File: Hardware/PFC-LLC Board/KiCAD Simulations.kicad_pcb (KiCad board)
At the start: 2 copper layers, 28 parts, among them Q1 C2M0160120D, U1 UCC28180DR

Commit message: Start of PCB
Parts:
- added C16: 220p, Capacitor_SMD:C_0402_1005Metric_Pad0.74x0.62mm_HandSolder, F.Cu at (81.3, 69.8)
- added Cboot1: 220n, Capacitor_SMD:C_0603_1608Metric_Pad1.08x0.95mm_HandSolder, F.Cu at (87.6, 221.0)
- added Cbw1: 3.9p, Capacitor_SMD:C_0402_1005Metric_Pad0.74x0.62mm_HandSolder, F.Cu at (42.5, 246.0)
- added Ccomp3: 390n, Capacitor_SMD:C_1206_3216Metric_Pad1.33x1.80mm_HandSolder, F.Cu at (67.3, 221.4)
- added Cin2: 47u, Capacitor_THT:CP_Radial_D25.0mm_P10.00mm_SnapIn, F.Cu at (47.0, 58.6)
- added Cinx1: 1.5u, Capacitor_THT:C_Rect_L26.5mm_W10.5mm_P22.50mm_MKS4, F.Cu at (71.1, 52.4)
- added Cisns1: 3.3p, Capacitor_SMD:C_0402_1005Metric_Pad0.74x0.62mm_HandSolder, F.Cu at (108.7, 127.0)
- added Cisns2: 150p, LLC_Cisns2:FA26C0G2J151JNU00, F.Cu at (157.5, 50.8)
- added Cout21: 120u, LLC_Cout:35SVPF120M, F.Cu at (242.6, 24.1)
- added Cout22: 120u, LLC_Cout:35SVPF120M, F.Cu at (242.6, 38.1)
- added Cout23: 120u, LLC_Cout:35SVPF120M, F.Cu at (242.6, 50.8)
- added Cout24: 120u, LLC_Cout:35SVPF120M, F.Cu at (242.6, 63.5)
- added Cout25: 120u, LLC_Cout:35SVPF120M, F.Cu at (242.6, 76.2)
- added Cout26: 120u, LLC_Cout:35SVPF120M, F.Cu at (243.1, 88.9)
- added Coutx21: 22u, Capacitor_SMD:C_0805_2012Metric_Pad1.18x1.45mm_HandSolder, F.Cu at (259.1, 31.8)
- added Coutx22: 22u, Capacitor_SMD:C_0805_2012Metric_Pad1.18x1.45mm_HandSolder, F.Cu at (259.3, 39.4)
- added Coutx23: 22u, Capacitor_SMD:C_0805_2012Metric_Pad1.18x1.45mm_HandSolder, F.Cu at (259.1, 45.7)
- added Coutx24: 22u, Capacitor_SMD:C_0805_2012Metric_Pad1.18x1.45mm_HandSolder, F.Cu at (259.1, 52.1)
- added Cr1: 33.454n, Capacitor_THT:C_Rect_L13.0mm_W5.0mm_P10.00mm_FKS3_FKP3_MKS4, F.Cu at (127.0, 50.8)
- added Cr2: 33.454n, Capacitor_THT:C_Rect_L13.0mm_W5.0mm_P10.00mm_FKS3_FKP3_MKS4, F.Cu at (127.0, 64.8)
- added Creg1: 2.2u, Capacitor_SMD:C_0402_1005Metric_Pad0.74x0.62mm_HandSolder, F.Cu at (181.6, 66.0)
- added Crvcc2: 4.7u, Capacitor_SMD:C_0805_2012Metric_Pad1.18x1.45mm_HandSolder, F.Cu at (52.0, 234.5)
- added Css1: 47n, Capacitor_SMD:C_0402_1005Metric_Pad0.74x0.62mm_HandSolder, F.Cu at (60.2, 231.9)
- added Css11: 47n, Capacitor_SMD:C_0402_1005Metric_Pad0.74x0.62mm_HandSolder, F.Cu at (109.9, 259.7)
- added Css12: 47n, Capacitor_SMD:C_0402_1005Metric_Pad0.74x0.62mm_HandSolder, F.Cu at (113.1, 259.7)
- added Css13: 47n, Capacitor_SMD:C_0402_1005Metric_Pad0.74x0.62mm_HandSolder, F.Cu at (98.5, 237.6)
- added Cvcc21: 15u, Capacitor_SMD:CP_Elec_5x5.8, F.Cu at (27.9, 134.6)
- added Cvcc22: 15u, Capacitor_SMD:CP_Elec_5x5.8, F.Cu at (38.1, 134.6)
- added Cvcc23: 15u, Capacitor_SMD:CP_Elec_5x5.8, F.Cu at (48.3, 134.6)
- added Cvcc24: 15u, Capacitor_SMD:CP_Elec_5x5.8, F.Cu at (58.4, 134.6)
- added Cvcc25: 15u, Capacitor_SMD:CP_Elec_5x5.8, F.Cu at (68.6, 134.6)
- added Cvcc26: 15u, Capacitor_SMD:CP_Elec_5x5.8, F.Cu at (78.7, 134.6)
- added Cvcc27: 15u, Capacitor_SMD:CP_Elec_5x5.8, F.Cu at (88.9, 134.6)
- added Cvcc28: 15u, Capacitor_SMD:CP_Elec_5x5.8, F.Cu at (99.1, 134.6)
- added Cvcc3: 2.2u, Capacitor_SMD:C_0805_2012Metric_Pad1.18x1.45mm_HandSolder, F.Cu at (109.2, 134.6)
- added Cvcr1: 66.044p, Capacitor_THT:C_Rect_L7.2mm_W4.5mm_P5.00mm_FKS2_FKP2_MKS2_MKP2, F.Cu at (144.9, 57.1)
- added Cvcr2: 1n, Capacitor_SMD:C_0805_2012Metric_Pad1.18x1.45mm_HandSolder, F.Cu at (48.1, 240.5)
- added Cvcr21: 1n, Capacitor_SMD:C_0805_2012Metric_Pad1.18x1.45mm_HandSolder, F.Cu at (147.3, 66.0)
- added Cvcr22: 1n, Capacitor_SMD:C_0805_2012Metric_Pad1.18x1.45mm_HandSolder, F.Cu at (147.3, 71.1)
- added Cvcr23: 1n, Capacitor_SMD:C_0805_2012Metric_Pad1.18x1.45mm_HandSolder, F.Cu at (147.3, 74.9)
- added Cvcr24: 1n, Capacitor_SMD:C_0805_2012Metric_Pad1.18x1.45mm_HandSolder, F.Cu at (147.6, 80.0)
- added Cvcr25: 1n, Capacitor_SMD:C_0805_2012Metric_Pad1.18x1.45mm_HandSolder, F.Cu at (147.3, 85.1)
- added Cvcr26: 1n, Capacitor_SMD:C_0805_2012Metric_Pad1.18x1.45mm_HandSolder, F.Cu at (147.6, 90.2)
- added Cvrcc1: 4.7u, Capacitor_SMD:C_0805_2012Metric_Pad1.18x1.45mm_HandSolder, F.Cu at (43.3, 243.5)
- added Cz1: 100n, Capacitor_SMD:C_0603_1608Metric_Pad1.08x0.95mm_HandSolder, F.Cu at (83.3, 221.0)
- added Dboot1: DIODE, DO-214BA:DO-214BA, F.Cu at (55.0, 254.1)
- added Dz1: BZX84Cxx, Diode_SMD:D_SOT-23_ANK, F.Cu at (52.8, 241.2)
- added J1: Conn_01x02_Female, Connector_PinHeader_1.27mm:PinHeader_1x02_P1.27mm_Vertical, F.Cu at (110.5, -39.4)
- added J2: Conn_01x02_Female, Connector_PinHeader_1.27mm:PinHeader_1x02_P1.27mm_Vertical, F.Cu at (47.8, 243.7)
- added J3: Conn_01x02_Female, Connector_PinHeader_1.27mm:PinHeader_1x02_P1.27mm_Vertical, F.Cu at (56.5, 232.0)
- added QM1: IPP060N06N, Package_TO_SOT_THT:TO-220-3_Vertical, F.Cu at (113.0, 52.1)
- added QM2: IPP060N06N, Package_TO_SOT_THT:TO-220-3_Vertical, F.Cu at (113.0, 66.0)
- added QM3: C2M0025120D, Package_TO_SOT_THT:TO-247-3_Vertical, F.Cu at (172.7, 53.3)
- added QM4: C2M0025120D, Package_TO_SOT_THT:TO-247-3_Vertical, F.Cu at (215.5, 66.0)
- added R19: 121k, Resistor_SMD:R_0402_1005Metric_Pad0.72x0.64mm_HandSolder, F.Cu at (81.3, 67.3)
- added R20: 4.99M, Resistor_SMD:R_1206_3216Metric_Pad1.30x1.75mm_HandSolder, F.Cu at (82.3, 52.1)
- added R27: 4.99M, Resistor_SMD:R_1206_3216Metric_Pad1.30x1.75mm_HandSolder, F.Cu at (82.3, 62.2)
- added R28: 4.99M, Resistor_SMD:R_1206_3216Metric_Pad1.30x1.75mm_HandSolder, F.Cu at (82.3, 57.1)
- added Rbias1: 6.04k, Resistor_SMD:R_0402_1005Metric_Pad0.72x0.64mm_HandSolder, F.Cu at (66.0, 211.8)
- added Rboot1: 2.20, Resistor_SMD:R_0805_2012Metric_Pad1.20x1.40mm_HandSolder, F.Cu at (52.0, 237.4)
- added Rbw1: 35.7k, Resistor_SMD:R_0402_1005Metric_Pad0.72x0.64mm_HandSolder, F.Cu at (161.3, 66.0)
- added Rbw2: 10k, Resistor_SMD:R_0201_0603Metric_Pad0.64x0.40mm_HandSolder, F.Cu at (161.3, 72.4)
- added Rcomp2: 44.2k, Resistor_SMD:R_0201_0603Metric_Pad0.64x0.40mm_HandSolder, F.Cu at (72.2, 211.7)
- added Rdrv1: 5.11k, Resistor_SMD:R_0402_1005Metric_Pad0.72x0.64mm_HandSolder, F.Cu at (97.8, 57.1)
- added Rdrv2: 5.11k, Resistor_SMD:R_0402_1005Metric_Pad0.72x0.64mm_HandSolder, F.Cu at (98.4, 67.3)
- added Rfbb2: 8.06k, Resistor_SMD:R_0402_1005Metric_Pad0.72x0.64mm_HandSolder, F.Cu at (69.2, 211.8)
- added Rfbt4: 110k, Resistor_SMD:R_0603_1608Metric_Pad0.98x0.95mm_HandSolder, F.Cu at (61.0, 252.5)
- added Rho1: 1, Resistor_SMD:R_0402_1005Metric_Pad0.72x0.64mm_HandSolder, F.Cu at (98.4, 52.1)
- added Risns1: 80.759, Resistor_SMD:R_0603_1608Metric_Pad0.98x0.95mm_HandSolder, F.Cu at (157.8, 57.1)
- added Rled1: 36.5k, Resistor_SMD:R_0201_0603Metric_Pad0.64x0.40mm_HandSolder, F.Cu at (75.0, 211.7)
- added Rlimit1: 18.2k, Resistor_SMD:R_1206_3216Metric_Pad1.30x1.75mm_HandSolder, F.Cu at (73.3, 221.4)
- added Rlo1: 1, Resistor_SMD:R_0402_1005Metric_Pad0.72x0.64mm_HandSolder, F.Cu at (98.4, 62.2)
- added Rvcc1: 44.2k, Resistor_SMD:R_0201_0603Metric_Pad0.64x0.40mm_HandSolder, F.Cu at (60.0, 233.8)
- added Rvcc2: 12.1k, Resistor_SMD:R_0201_0603Metric_Pad0.64x0.40mm_HandSolder, F.Cu at (55.8, 237.8)
- added U1LLC1: UCC256403DDBR, LLC_U1:UCC256403DDBR, F.Cu at (101.6, 94.0)
- added U2LLC1: UCC24624DT, LLC_U2:UCC24624DT, F.Cu at (199.4, 62.2)
- added UO1: PS2501L-1-F3-A, LLC_O1:PS2501L-1-F3-A, F.Cu at (157.5, 208.3)
- added UVR1: TLV431AIDBVT, LLC_VR1:TLV431AIDBVT, F.Cu at (71.6, 243.9)
- moved Ccomp1 146.8 mm to (76.2, -61.0)
- moved Ccomp2 146.8 mm to (88.0, -64.4)
- moved Cicomp1 146.8 mm to (81.0, -61.0)
- moved Cin1 146.8 mm to (76.2, -58.0)
- moved Cisense1 146.8 mm to (83.3, -56.8)
- moved Cvcc1 146.8 mm to (70.8, -60.8)
- moved Cvsense1 146.8 mm to (83.3, -58.6)
- moved Dac1 146.8 mm to (95.9, -67.0)
- moved Dboost1 146.8 mm to (87.6, -53.3)
- moved Disense1 146.8 mm to (117.0, -67.7)
- moved Dstart1 146.8 mm to (87.6, -41.9)
- moved Dturnoff1 146.8 mm to (142.6, -52.1)
- moved Q1 146.8 mm to (115.0, -60.9)
- moved Rcomp1 146.8 mm to (80.0, -56.6)
- moved Rfbb1 146.8 mm to (91.0, -66.5)
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
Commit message: Schematic/PCB updates
Minor updates to schematic and some place of PCB components as been done
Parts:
- removed Css1: 47n, Capacitor_SMD:C_0402_1005Metric_Pad0.74x0.62mm_HandSolder
- removed Dac1: GBU8M, Diode_THT:Diode_Bridge_Vishay_GBU
- removed the U1 at (132.5, -41.4)
- moved Cout21 221.3 mm to (268.7, 243.8), turned to 270 degrees
- moved Cout22 206.2 mm to (256.0, 243.8), turned to 270 degrees
- moved Cout23 193.0 mm to (243.3, 243.8), turned to 270 degrees
- moved Rbw1 191.2 mm to (94.2, 245.1), turned to 180 degrees
- moved Rbw2 183.9 mm to (94.1, 243.6)
- moved Cvcc28 181.6 mm to (31.0, 303.0), turned to 270 degrees
- moved Coutx21 181.6 mm to (278.4, 212.3)
- moved Coutx22 178.1 mm to (278.4, 216.4)
- moved Rho1 176.5 mm to (100.0, 228.6)
- moved Coutx23 175.8 mm to (278.4, 220.5)
- moved Cvcc27 175.0 mm to (41.1, 303.0), turned to 270 degrees
- moved Cr1 174.5 mm to (113.8, 224.8), turned to 270 degrees
- moved Coutx24 173.5 mm to (278.4, 224.5)
- moved Rlo1 173.0 mm to (100.1, 235.2)
- moved Cvcc26 170.6 mm to (51.3, 303.0), turned to 270 degrees
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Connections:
- Ccomp2 pad 2: Net-(Ccomp2-Pad2) -> GND
- Cicomp1 pad 2: Net-(Ccomp2-Pad2) -> GND
- Cisense1 pad 2: Net-(Ccomp2-Pad2) -> GND
- Cvcc1 pad 2: Net-(Ccomp2-Pad2) -> GND
- Cvccx1 pad 2: Net-(Ccomp2-Pad2) -> GND
- Cvsense1 pad 2: Net-(Ccomp2-Pad2) -> GND
- Disense1 pad 2: Net-(Ccomp2-Pad2) -> GND
- J1 pad 1: Net-(Ccomp2-Pad2) -> GND
- Rcomp1 pad 2: Net-(Ccomp2-Pad2) -> GND
- Rfbb1 pad 2: Net-(Ccomp2-Pad2) -> GND
- Rfreq1 pad 2: Net-(Ccomp2-Pad2) -> GND
- U1 pad 1: Net-(Ccomp2-Pad2) -> GND

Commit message: All footprints except PFC output caps
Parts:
- removed Cvcr2: 1n, Capacitor_SMD:C_0805_2012Metric_Pad1.18x1.45mm_HandSolder
- removed J1, J2, J3: Conn_01x02_Female, Connector_PinHeader_1.27mm:PinHeader_1x02_P1.27mm_Vertical
- added L1: 148.268u, PFC_L1:IND_FIT106-2, F.Cu at (275.6, -52.6)
- added Lr1: PA4344.473ANLT, LLC_Lr:PA4344.473ANLT, F.Cu at (331.2, 117.3)
- added Rntc1: 1, Resistor_THT:R_Box_L13.0mm_W4.0mm_P9.00mm, F.Cu at (187.2, -19.8)
- added TR1: TRANSF6, LLC_T1:EPCOS-B65982E0012D001-MFG, F.Cu at (351.5, 49.8)
- moved Cvcc24 220.3 mm to (181.9, 133.6), turned to 90 degrees
- moved Cvcc23 206.9 mm to (171.7, 133.6), turned to 90 degrees
- moved Rvcc1 201.6 mm to (198.4, 145.6)
- moved Css11 200.9 mm to (193.3, 145.5)
- moved Css12 200.9 mm to (190.8, 145.5)
- moved Css13 200.9 mm to (188.2, 145.5)
- moved Rvcc2 200.9 mm to (195.8, 145.6)
- moved Cbw1 200.5 mm to (197.1, 132.0)
- moved Cisns1 200.5 mm to (193.3, 132.0)
- moved Crvcc2 200.5 mm to (194.3, 137.7)
- moved Cvcc25 200.5 mm to (181.9, 142.7)
- moved Cvcc26 200.5 mm to (171.7, 142.7)
- moved Cvcc27 200.5 mm to (161.5, 142.7)
- moved Cvcc28 200.5 mm to (151.4, 142.7)
- moved Cvcc3 200.5 mm to (189.5, 132.4)
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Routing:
- net GND: track 0.00 -> 59.6 mm
- net Net-(Cvcr1-Pad2): track 0.00 -> 27.7 mm
- net Net-(Rbias1-Pad1): track 0.00 -> 25.0 mm
- net Net-(Rbias1-Pad2): track 0.00 -> 22.7 mm
- net Net-(Cz1-Pad1): track 0.00 -> 16.6 mm
- net Net-(Ccomp3-Pad1): track 0.00 -> 15.9 mm
- net Net-(Css11-Pad1): track 0.00 -> 10.2 mm
- net Net-(Crvcc2-Pad1): track 0.00 -> 9.38 mm
- net Net-(Rfbb2-Pad2): track 0.00 -> 5.39 mm
- net Net-(Cz1-Pad2): track 0.00 -> 4.96 mm
- net Net-(Ccomp3-Pad2): track 0.00 -> 3.73 mm
- net Net-(Cout21-Pad1): track 0.00 -> 3.11 mm
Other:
- board outline added: 217.4 x 136.9 mm

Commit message: missing 4 PFC components
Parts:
- added J1: 1792229, Connector2x1:PHOENIX_1792229, F.Cu at (148.6, -30.5)
- added J2: Conn_01x02_Female, Connector_PinHeader_1.27mm:PinHeader_1x02_P1.27mm_Vertical, F.Cu at (243.3, -26.2)
- added J3: 1792229, Connector2x1:PHOENIX_1792229, F.Cu at (266.2, -17.0)
- added J4: 1792229, Connector2x1:PHOENIX_1792229, F.Cu at (114.6, 136.9)
- added J5: Conn_01x02_Female, Connector_PinHeader_1.27mm:PinHeader_1x02_P1.27mm_Vertical, F.Cu at (141.0, 132.8)
- added J6: 1792229, Connector2x1:PHOENIX_1792229, F.Cu at (114.8, 113.0)
- moved Lr1 140.8 mm to (197.9, 72.1), turned to 270 degrees
- moved TR1 116.9 mm to (238.3, 78.5), turned to 0 degrees
- moved Cout24 30.4 mm to (128.3, 83.6)
- moved Cout25 30.4 mm to (141.0, 83.6)
- moved Cout26 30.4 mm to (115.6, 83.6)
- moved Cout21 30.4 mm to (115.6, 98.0)
- moved Cout22 30.4 mm to (128.3, 98.0)
- moved Cout23 30.4 mm to (141.0, 98.0)
- moved QM3 29.8 mm to (160.3, 53.1)
- moved QM4 29.8 mm to (181.6, 53.1)
- moved Coutx21 29.4 mm to (152.7, 80.3)
- moved Coutx22 29.4 mm to (156.7, 80.3)
- moved Coutx23 29.4 mm to (160.8, 80.3)
- moved Coutx24 29.4 mm to (164.8, 80.3)
- moved Creg1 27.7 mm to (167.1, 75.2)
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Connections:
- Cout21 pad 2: Net-(Cout21-Pad2) -> GND1
- Cout22 pad 2: Net-(Cout21-Pad2) -> GND1
- Cout23 pad 2: Net-(Cout21-Pad2) -> GND1
- Cout24 pad 2: Net-(Cout21-Pad2) -> GND1
- Cout25 pad 2: Net-(Cout21-Pad2) -> GND1
- Cout26 pad 2: Net-(Cout21-Pad2) -> GND1
- Coutx21 pad 2: Net-(Cout21-Pad2) -> GND1
- Coutx22 pad 2: Net-(Cout21-Pad2) -> GND1
- Coutx23 pad 2: Net-(Cout21-Pad2) -> GND1
- Coutx24 pad 2: Net-(Cout21-Pad2) -> GND1
- Creg1 pad 2: Net-(Cout21-Pad2) -> GND1
- Cz1 pad 2: Net-(Cz1-Pad2) -> GND1
- Dz1 pad 2: Net-(Cz1-Pad2) -> GND1
- QM3 pad 2: Net-(Cout21-Pad2) -> GND1
- QM4 pad 3: Net-(Cout21-Pad2) -> GND1
- Rfbb2 pad 2: Net-(Rfbb2-Pad2) -> GND1
- U2LLC1 pad 2: Net-(Cout21-Pad2) -> GND1
- U2LLC1 pad 5: Net-(Cout21-Pad2) -> GND1
- UVR1 pad 5: Net-(Rfbb2-Pad2) -> GND1
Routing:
- net GND1: track 0.00 -> 10.3 mm
- net Net-(Rfbb2-Pad2): track 5.39 -> 0.00 mm
- net Net-(Cz1-Pad2): track 4.96 -> 0.00 mm

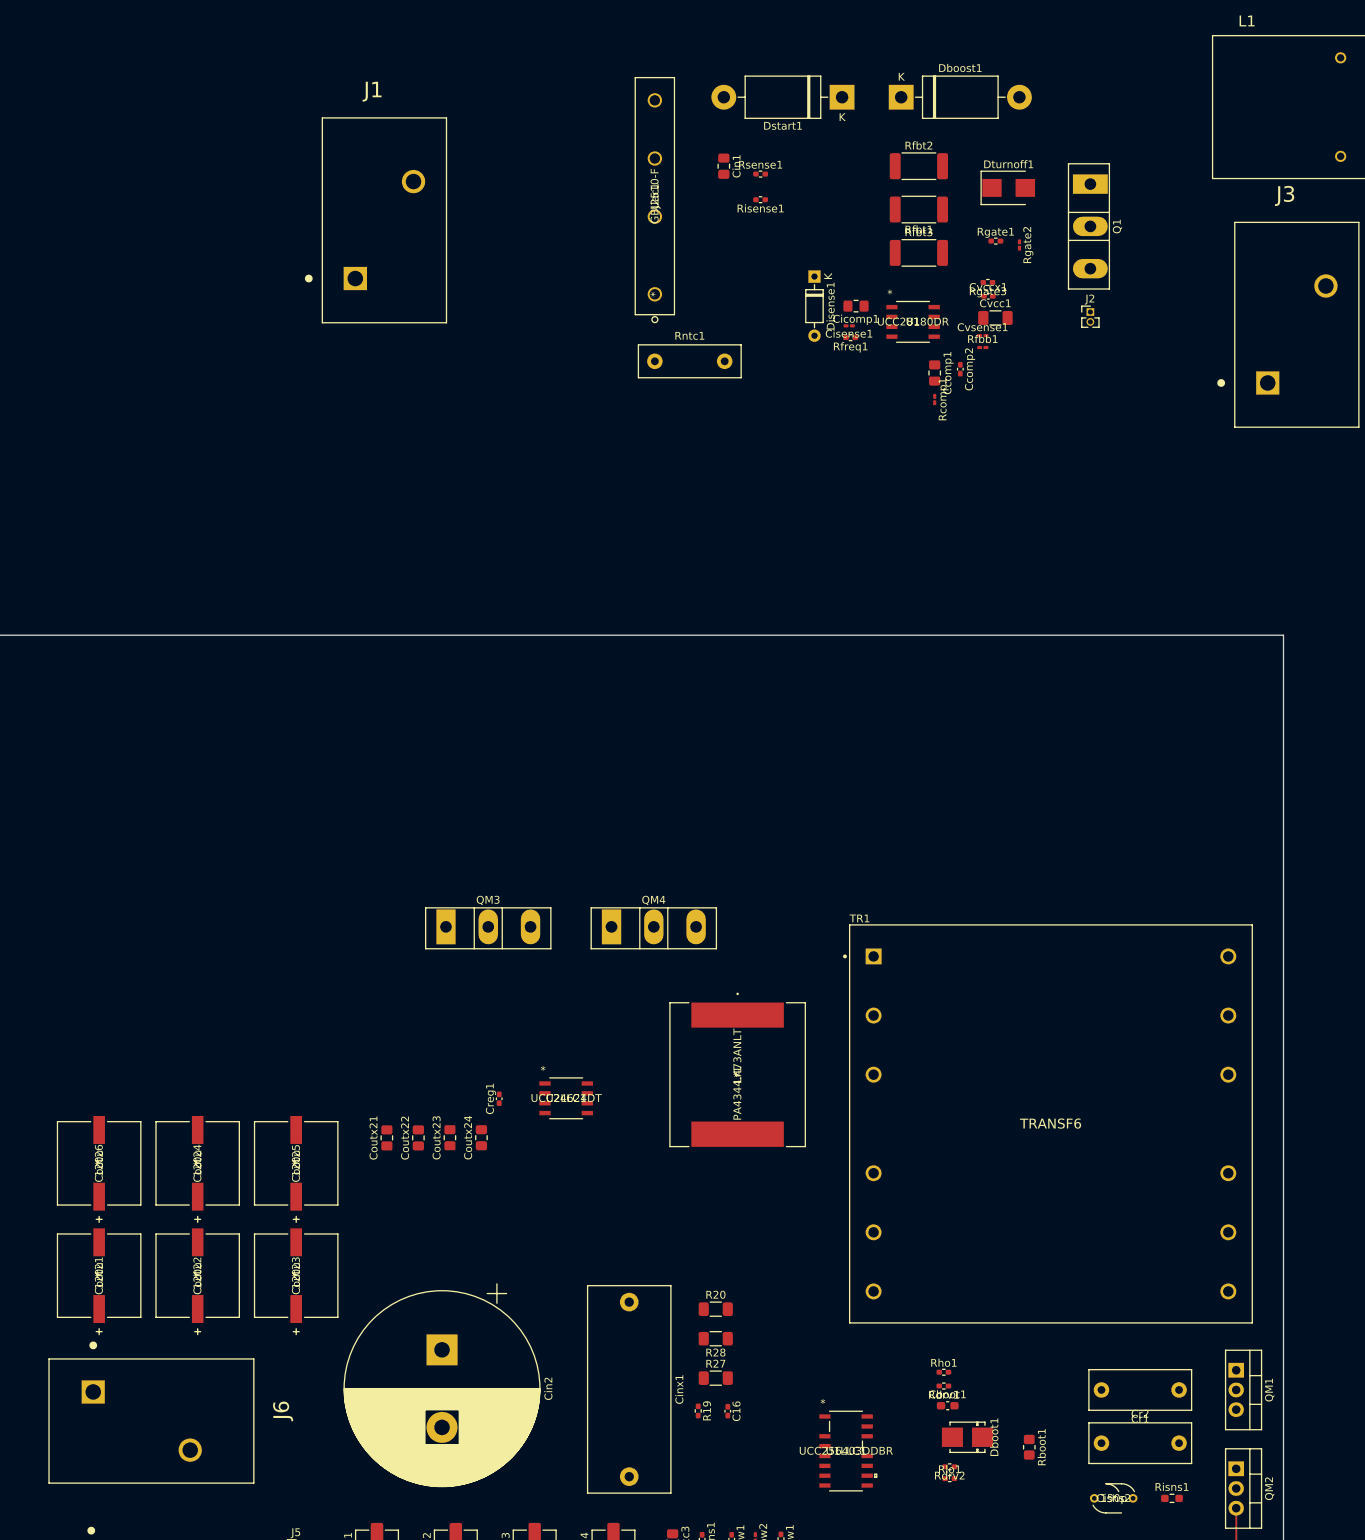
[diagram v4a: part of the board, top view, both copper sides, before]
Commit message: All component footprints found and ready for PCB layout
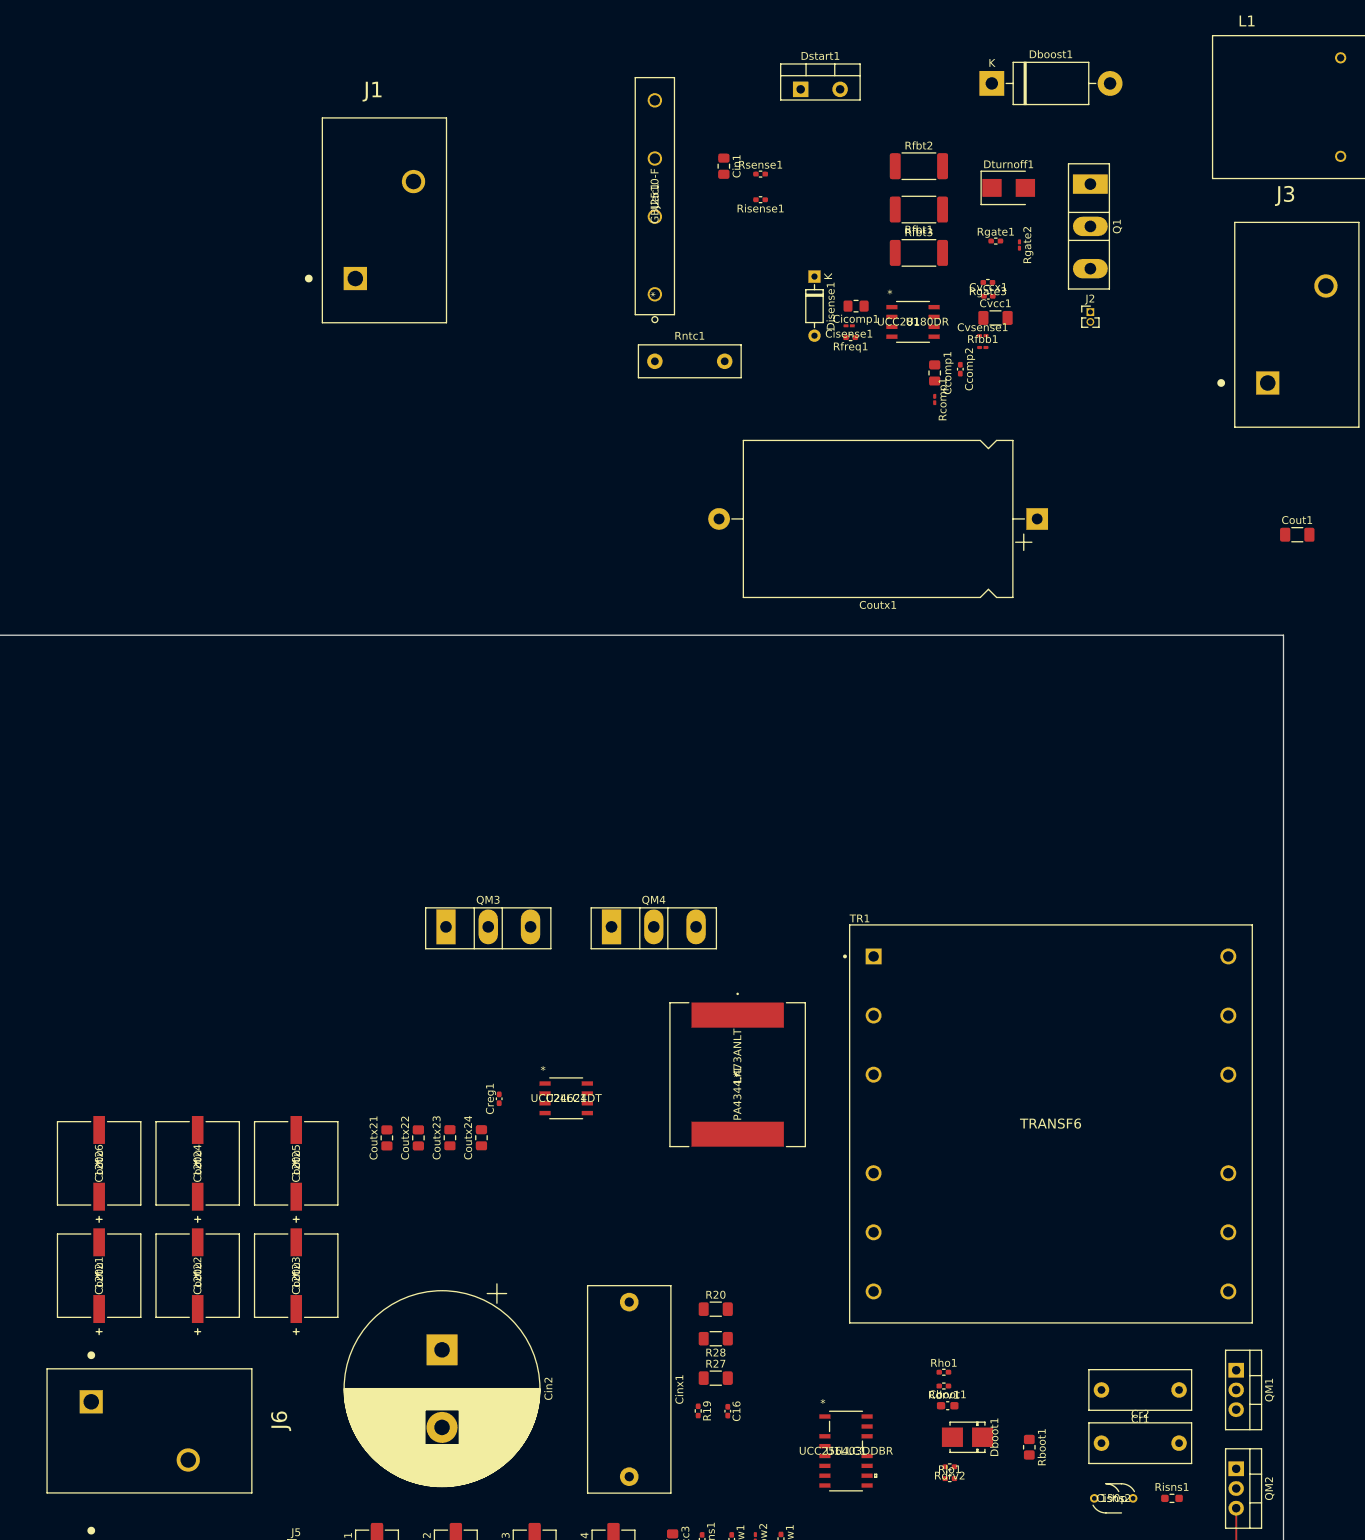
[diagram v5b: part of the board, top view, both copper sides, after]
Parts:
- added Cout1: 18.113m, Capacitor_SMD:C_1206_3216Metric_Pad1.33x1.80mm_HandSolder, F.Cu at (270.0, 2.54)
- added Coutx1: 100n, Capacitor_THT:CP_Axial_L34.5mm_D20.0mm_P41.00mm_Horizontal, F.Cu at (236.5, 0.51)
- Dboost1: value 1N5406 -> UF5406
- Dstart1: value 1N5406 -> C3D10060A; footprint Diode_THT:D_DO-201AD_P15.24mm_Horizontal -> Package_TO_SOT_THT:TO-220-2_Vertical
- moved Dboost1 11.8 mm to (230.6, -55.6)
- moved Dstart1 5.43 mm to (206.0, -54.9), turned to 0 degrees
- moved J6 1.30 mm to (114.6, 114.3)

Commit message: initial layout
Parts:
- moved L1 234.1 mm to (72.4, 63.8)
- moved J2 213.5 mm to (57.4, 78.7)
- moved TR1 164.4 mm to (80.3, 124.0), turned to 180 degrees
- moved Dboost1 148.4 mm to (111.8, 33.3)
- moved Cvcr1 148.3 mm to (112.8, 76.2), turned to 0 degrees
- moved QM2 142.6 mm to (120.4, 138.9), turned to 180 degrees
- moved Cisns2 137.5 mm to (115.6, 84.3)
- moved Rgate1 135.7 mm to (124.6, 48.8)
- moved Rgate2 134.9 mm to (128.0, 48.4), turned to 90 degrees
- moved Q1 134.4 mm to (125.0, 21.1), turned to 0 degrees
- moved Rgate3 134.4 mm to (124.0, 52.4), turned to 270 degrees
- moved Rntc1 134.1 mm to (70.4, 46.0), turned to 180 degrees
- moved Disense1 131.6 mm to (100.8, 46.0), turned to 0 degrees
- moved Rfreq1 131.6 mm to (111.7, 61.7)
- moved Cicomp1 131.5 mm to (111.0, 55.9), turned to 90 degrees
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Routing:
- net GND: track 59.6 -> 0.08 mm
- net Net-(Cvcr1-Pad2): track 27.7 -> 0.14 mm
- net Net-(Rbias1-Pad1): track 25.0 -> 0.00 mm
- net Net-(Rbias1-Pad2): track 22.7 -> 0.11 mm
- net Net-(Cz1-Pad1): track 16.6 -> 0.12 mm
- net Net-(Ccomp3-Pad1): track 15.9 -> 0.00 mm
- net GND1: track 10.3 -> 0.00 mm
- net Net-(Css11-Pad1): track 10.2 -> 0.00 mm
- net Net-(Crvcc2-Pad1): track 9.38 -> 0.00 mm
- net Net-(Ccomp3-Pad2): track 3.73 -> 0.00 mm
- net Net-(Cout21-Pad1): track 3.11 -> 0.21 mm
